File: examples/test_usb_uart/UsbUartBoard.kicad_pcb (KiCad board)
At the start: 2 copper layers, 29 x 12 mm, 18 parts

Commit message: clean up protection
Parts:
- UD1: value (none) -> MMSZ5232A_R1_00001 (PANJIT International) - 5?A@3V 11? Single 5.49V~5.71V 500mW 5.6V SOD-123 Zener Diodes ROHS; footprint Diode_SMD:D_MiniMELF -> Diode_SMD:D_SOD-123
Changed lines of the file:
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@@
     (pad "" np_thru_hole circle locked (at 0 0) (size 1.152 1.152) (drill 1.152) (layers *.Cu *.Mask))
   )
-  (footprint "Diode_SMD:D_MiniMELF" (layer "F.Cu")
+  (footprint "Diode_SMD:D_SOD-123" (layer "F.Cu")
     (at 146 43)
-    (descr "Diode Mini-MELF (SOD-80)")
-    (tags "Diode Mini-MELF (SOD-80)")
-    (property "Sheetfile" "")
-    (property "Sheetname" "")
-    (property "edg_part" "TCLLZ5V6TR (Tak Cheong)")
+    (descr "SOD-123")
+    (tags "SOD-123")
+    (property "Sheetfile" "")
+    (property "Sheetname" "")
+    (property "edg_part" "MMSZ5232A_R1_00001 (PANJIT International)")
     (property "edg_path" "vusb_protect.diode")
     (property "edg_refdes" "UD1")
     (property "edg_short_path" "vusb_protect")
     (attr smd)
-    (fp_text reference "UD1" (at -3.5 0) (layer "F.SilkS")
+    (fp_text reference "UD1" (at -3 0) (layer "F.SilkS")
       (effects (font (size 0.8 0.6) (thickness 0.1)))
     )
-    (fp_text value "" (at 0 1.75) (layer "F.Fab")
+    (fp_text value "MMSZ5232A_R1_00001 (PANJIT International) - 5?A@3V 11? Single 5.49V~5.71V 500mW 5.6V SOD-123 Zener Diodes ROHS" (at 0 2.1) (layer "F.Fab")
       (effects (font (size 1 1) (thickness 0.15)))
     )
@@
       (effects (font (size 1 1) (thickness 0.15)))
     )
-    (fp_line (start 1.75 -1) (end -2.55 -1) (layer "F.SilkS") (width 0.12))
-    (fp_line (start -2.55 1) (end 1.75 1) (layer "F.SilkS") (width 0.12))
-    (fp_line (start -2.55 -1) (end -2.55 1) (layer "F.SilkS") (width 0.12))
-    (fp_line (start -2.65 -1.1) (end 2.65 -1.1) (layer "F.CrtYd") (width 0.05))
-    (fp_line (start 2.65 1.1) (end -2.65 1.1) (layer "F.CrtYd") (width 0.05))
-    (fp_line (start -2.65 1.1) (end -2.65 -1.1) (layer "F.CrtYd") (width 0.05))
-    (fp_line (start 2.65 -1.1) (end 2.65 1.1) (layer "F.CrtYd") (width 0.05))
-    (fp_line (start -1.65 -0.8) (end 1.65 -0.8) (layer "F.Fab") (width 0.1))
+    (fp_line (start -2.25 -1) (end 1.65 -1) (layer "F.SilkS") (width 0.12))
+    (fp_line (start -2.25 1) (end 1.65 1) (layer "F.SilkS") (width 0.12))
+    (fp_line (start -2.25 -1) (end -2.25 1) (layer "F.SilkS") (width 0.12))
+    (fp_line (start 2.35 1.15) (end -2.35 1.15) (layer "F.CrtYd") (width 0.05))
+    (fp_line (start -2.35 -1.15) (end 2.35 -1.15) (layer "F.CrtYd") (width 0.05))
+    (fp_line (start -2.35 -1.15) (end -2.35 1.15) (layer "F.CrtYd") (width 0.05))
+    (fp_line (start 2.35 -1.15) (end 2.35 1.15) (layer "F.CrtYd") (width 0.05))
+    (fp_line (start -1.4 0.9) (end -1.4 -0.9) (layer "F.Fab") (width 0.1))
+    (fp_line (start -0.35 0) (end 0.25 -0.4) (layer "F.Fab") (width 0.1))
+    (fp_line (start 0.25 -0.4) (end 0.25 0.4) (layer "F.Fab") (width 0.1))
+    (fp_line (start -1.4 -0.9) (end 1.4 -0.9) (layer "F.Fab") (width 0.1))
+    (fp_line (start 0.25 0.4) (end -0.35 0) (layer "F.Fab") (width 0.1))
+    (fp_line (start 1.4 -0.9) (end 1.4 0.9) (layer "F.Fab") (width 0.1))
+    (fp_line (start -0.35 0) (end -0.35 -0.55) (layer "F.Fab") (width 0.1))
+    (fp_line (start 1.4 0.9) (end -1.4 0.9) (layer "F.Fab") (width 0.1))
     (fp_line (start -0.35 0) (end -0.35 0.55) (layer "F.Fab") (width 0.1))
-    (fp_line (start -0.35 0) (end -0.35 -0.55) (layer "F.Fab") (width 0.1))
+    (fp_line (start 0.25 0) (end 0.75 0) (layer "F.Fab") (width 0.1))
     (fp_line (start -0.75 0) (end -0.35 0) (layer "F.Fab") (width 0.1))
-    (fp_line (start 0.25 0) (end 0.75 0) (layer "F.Fab") (width 0.1))
-    (fp_line (start 0.25 -0.4) (end 0.25 0.4) (layer "F.Fab") (width 0.1))
-    (fp_line (start 0.25 0.4) (end -0.35 0) (layer "F.Fab") (width 0.1))
-    (fp_line (start -0.35 0) (end 0.25 -0.4) (layer "F.Fab") (width 0.1))
-    (fp_line (start -1.65 0.8) (end -1.65 -0.8) (layer "F.Fab") (width 0.1))
-    (fp_line (start 1.65 0.8) (end -1.65 0.8) (layer "F.Fab") (width 0.1))
-    (fp_line (start 1.65 -0.8) (end 1.65 0.8) (layer "F.Fab") (width 0.1))
-    (pad "1" smd rect (at -1.75 0) (size 1.3 1.7) (layers "F.Cu" "F.Paste" "F.Mask")
+    (pad "1" smd rect (at -1.65 0) (size 0.9 1.2) (layers "F.Cu" "F.Paste" "F.Mask")
       (net 3 "vusb"))
-    (pad "2" smd rect (at 1.75 0) (size 1.3 1.7) (layers "F.Cu" "F.Paste" "F.Mask")
+    (pad "2" smd rect (at 1.65 0) (size 0.9 1.2) (layers "F.Cu" "F.Paste" "F.Mask")
       (net 1 "gnd"))
-    (model "${KICAD6_3DMODEL_DIR}/Diode_SMD.3dshapes/D_MiniMELF.wrl"
+    (model "${KICAD6_3DMODEL_DIR}/Diode_SMD.3dshapes/D_SOD-123.wrl"
       (offset (xyz 0 0 0))
       (scale (xyz 1 1 1))
@@
     (fp_arc (start -0.573812 -0.957555) (mid 0.159981 -0.670103) (end 0.575946 -0.000734) (layer "B.Cu") (width 0.16))
     (fp_arc (start 0.286757 -1.643905) (mid 0.02807 -1.671353) (end -0.213115 -1.768832) (layer "B.Cu") (width 0.16))
-    (fp_arc (start 0.763205 0.913443) (mid 0.969127 0.866756) (end 1.178844 0.891296) (layer "B.Cu") (width 0.16))
+    (fp_arc (start 0.763205 0.913443) (mid 0.969127 0.866758) (end 1.178844 0.891296) (layer "B.Cu") (width 0.16))
     (fp_arc (start 0.320058 -1.56145) (mid 0.561228 -1.658966) (end 0.819911 -1.686455) (layer "B.Cu") (width 0.16))
     (fp_arc (start -0.303506 0.391461) (mid -0.661618 -0.021387) (end -0.809366 -0.547561) (layer "B.Cu") (width 0.2))
@@
     (fp_arc (start -0.303506 0.391461) (mid -0.117368 0.560252) (end 0.03125 0.762861) (layer "B.Cu") (width 0.2))
     (fp_arc (start -1.072198 -1.25) (mid -0.886856 -0.918958) (end -0.809364 -0.547562) (layer "B.Cu") (width 0.2))
-    (fp_arc (start 0.869178 1.169286) (mid 1.000175 1.003686) (end 1.178836 0.891151) (layer "B.Cu") (width 0.16))
+    (fp_arc (start 0.869178 1.169286) (mid 1.000176 1.003686) (end 1.178836 0.891151) (layer "B.Cu") (width 0.16))
     (fp_arc (start 1.093749 -1.89443) (mid 0.000001 2.187499) (end -1.09375 -1.894429) (layer "B.Cu") (width 0.2))
     (fp_circle (center 0.3125 1.25) (end 0.875 1.25) (layer "B.Cu") (width 0.2) (fill none))

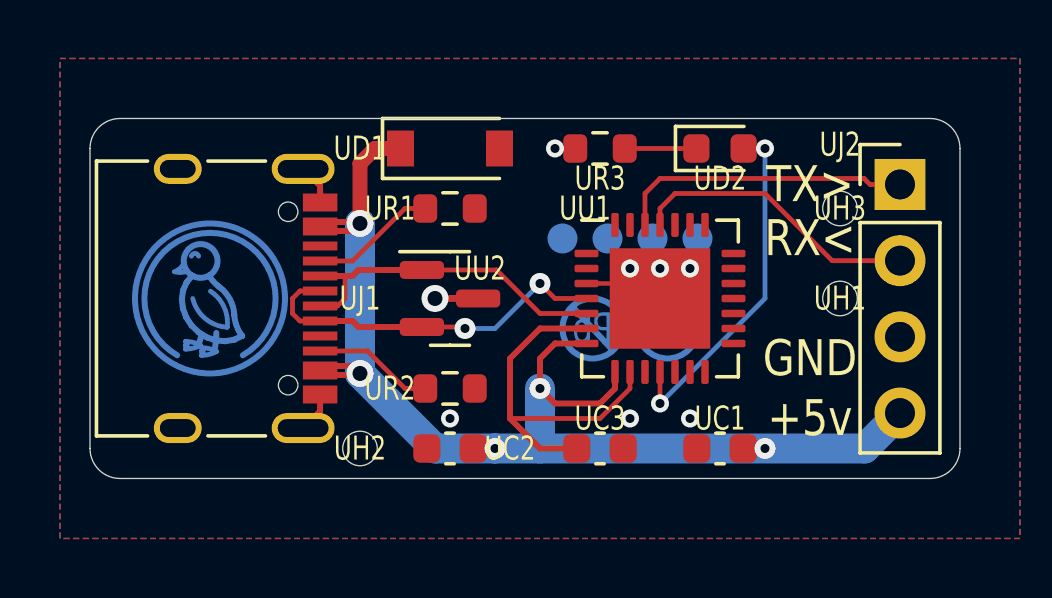
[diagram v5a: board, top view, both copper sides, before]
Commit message: update board art
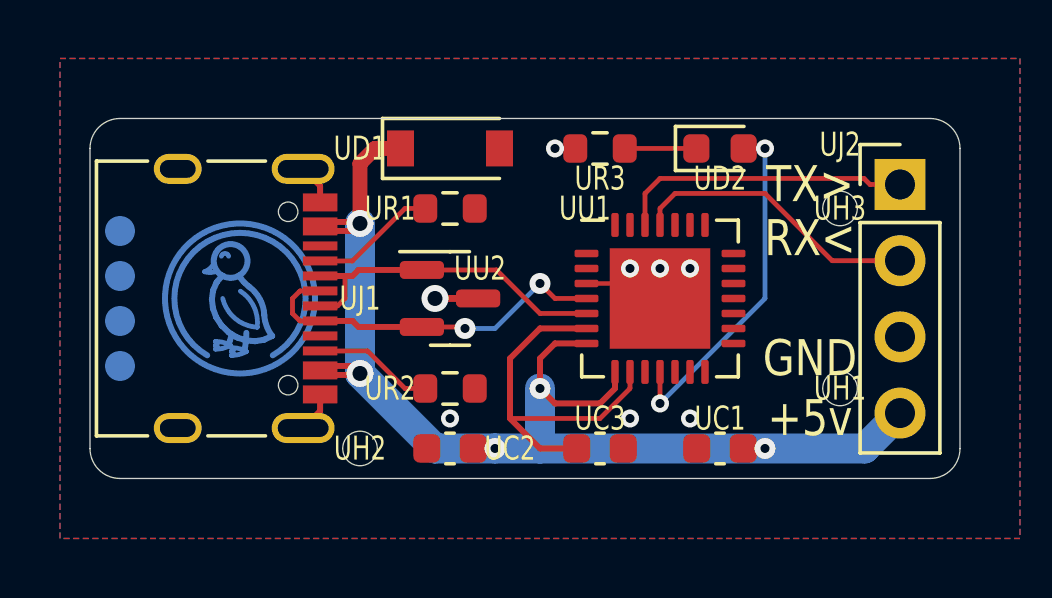
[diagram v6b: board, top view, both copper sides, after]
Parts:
- UU4: value LeadFree -> Lemur; footprint edg:Indicator_LeadFree -> edg:Symbol_LemurSmall
- moved UU5 17.1 mm to (135.0, 48.0), turned to 90 degrees
- moved UU4 8.06 mm to (144.0, 48.0)
- moved UH1 3.00 mm to (159.0, 51.0)
- moved UU3 1.00 mm to (139.0, 48.0)
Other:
- board text added: "CP2102 USB-UART Jan '23"

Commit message: fix usb diode
ESD5V3AL exceeds USB capacitance limits
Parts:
- UU2: value ESDA5V3L (STMicroelectronics) -> PGB102ST23 (Littelfuse)
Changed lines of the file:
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@@
     (property "Sheetfile" "")
     (property "Sheetname" "")
-    (property "edg_part" "ESDA5V3L (STMicroelectronics)")
+    (property "edg_part" "PGB102ST23 (Littelfuse)")
     (property "edg_path" "usb_esd")
     (property "edg_refdes" "UU2")
@@
       (effects (font (size 0.8 0.6) (thickness 0.1)))
     )
-    (fp_text value "ESDA5V3L (STMicroelectronics)" (at 0 2.4) (layer "F.Fab")
+    (fp_text value "PGB102ST23 (Littelfuse)" (at 0 2.4) (layer "F.Fab")
       (effects (font (size 1 1) (thickness 0.15)))
     )
@@
     (fp_arc (start -0.573812 -0.957555) (mid 0.159981 -0.670103) (end 0.575946 -0.000734) (layer "B.Cu") (width 0.16))
     (fp_arc (start 0.286757 -1.643905) (mid 0.02807 -1.671353) (end -0.213115 -1.768832) (layer "B.Cu") (width 0.16))
-    (fp_arc (start 0.763205 0.913443) (mid 0.969128 0.866757) (end 1.178844 0.891296) (layer "B.Cu") (width 0.16))
+    (fp_arc (start 0.763205 0.913443) (mid 0.969127 0.866756) (end 1.178844 0.891296) (layer "B.Cu") (width 0.16))
     (fp_arc (start 0.320058 -1.56145) (mid 0.561228 -1.658966) (end 0.819911 -1.686455) (layer "B.Cu") (width 0.16))
     (fp_arc (start -0.303506 0.391461) (mid -0.661618 -0.021387) (end -0.809366 -0.547561) (layer "B.Cu") (width 0.2))
@@
     (fp_arc (start -0.303506 0.391461) (mid -0.117368 0.560252) (end 0.03125 0.762861) (layer "B.Cu") (width 0.2))
     (fp_arc (start -1.072198 -1.25) (mid -0.886856 -0.918958) (end -0.809364 -0.547562) (layer "B.Cu") (width 0.2))
-    (fp_arc (start 0.869178 1.169286) (mid 1.000175 1.003684) (end 1.178836 0.891151) (layer "B.Cu") (width 0.16))
+    (fp_arc (start 0.869178 1.169286) (mid 1.000175 1.003685) (end 1.178836 0.891151) (layer "B.Cu") (width 0.16))
     (fp_arc (start 1.093749 -1.89443) (mid 0.000001 2.187499) (end -1.09375 -1.894429) (layer "B.Cu") (width 0.2))
     (fp_circle (center 0.3125 1.25) (end 0.875 1.25) (layer "B.Cu") (width 0.2) (fill none))

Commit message: layout cleanup + recoloring
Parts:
- UD2: value KT-0603R (Hubei KENTO Elec) - Red 615~630nm 1.9~2.2V 0603 Light Emitting Diodes (LED) RoHS -> C2290 (Hubei KENTO Elec) - White 0603 Light Emitting Diodes (LED) RoHS
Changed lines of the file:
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@@
     (property "Sheetfile" "electronics_abstract_parts.AbstractLed.IndicatorLed")
     (property "Sheetname" "led")
-    (property "edg_part" "KT-0603R (Hubei KENTO Elec)")
+    (property "edg_part" "C2290 (Hubei KENTO Elec)")
     (property "edg_path" "led.package")
     (property "edg_refdes" "UD2")
@@
       (effects (font (size 0.8 0.6) (thickness 0.1)))
     )
-    (fp_text value "KT-0603R (Hubei KENTO Elec) - Red 615~630nm 1.9~2.2V 0603 Light Emitting Diodes (LED) RoHS" (at 0 1.43) (layer "F.Fab")
+    (fp_text value "C2290 (Hubei KENTO Elec) - White 0603 Light Emitting Diodes (LED) RoHS" (at 0 1.43) (layer "F.Fab")
       (effects (font (size 1 1) (thickness 0.15)))
     )
@@
     (fp_arc (start -0.573812 -0.957555) (mid 0.159981 -0.670103) (end 0.575946 -0.000734) (layer "B.Cu") (width 0.16))
     (fp_arc (start 0.286757 -1.643905) (mid 0.02807 -1.671353) (end -0.213115 -1.768832) (layer "B.Cu") (width 0.16))
-    (fp_arc (start 0.763205 0.913443) (mid 0.969127 0.866756) (end 1.178844 0.891296) (layer "B.Cu") (width 0.16))
+    (fp_arc (start 0.763205 0.913443) (mid 0.969127 0.866758) (end 1.178844 0.891296) (layer "B.Cu") (width 0.16))
     (fp_arc (start 0.320058 -1.56145) (mid 0.561228 -1.658966) (end 0.819911 -1.686455) (layer "B.Cu") (width 0.16))
     (fp_arc (start -0.303506 0.391461) (mid -0.661618 -0.021387) (end -0.809366 -0.547561) (layer "B.Cu") (width 0.2))
@@
     (fp_arc (start -0.303506 0.391461) (mid -0.117368 0.560252) (end 0.03125 0.762861) (layer "B.Cu") (width 0.2))
     (fp_arc (start -1.072198 -1.25) (mid -0.886856 -0.918958) (end -0.809364 -0.547562) (layer "B.Cu") (width 0.2))
-    (fp_arc (start 0.869178 1.169286) (mid 1.000175 1.003685) (end 1.178836 0.891151) (layer "B.Cu") (width 0.16))
+    (fp_arc (start 0.869178 1.169286) (mid 1.000175 1.003686) (end 1.178836 0.891151) (layer "B.Cu") (width 0.16))
     (fp_arc (start 1.093749 -1.89443) (mid 0.000001 2.187499) (end -1.09375 -1.894429) (layer "B.Cu") (width 0.2))
     (fp_circle (center 0.3125 1.25) (end 0.875 1.25) (layer "B.Cu") (width 0.2) (fill none))
